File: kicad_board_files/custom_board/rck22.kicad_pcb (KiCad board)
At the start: 2 copper layers, 95.3 x 69.9 mm, 61 parts, among them CON1 Nokia1616_LCD, IC1 PEC11L-4115F-S0020, J1 Conn_02x05_Odd_Even, J2 USB_OTG, J3 Thermocouple, J4 5V_DC_IN, J6 SSR, Q1 BC547, Q2 BSS138, SW1 PTS810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

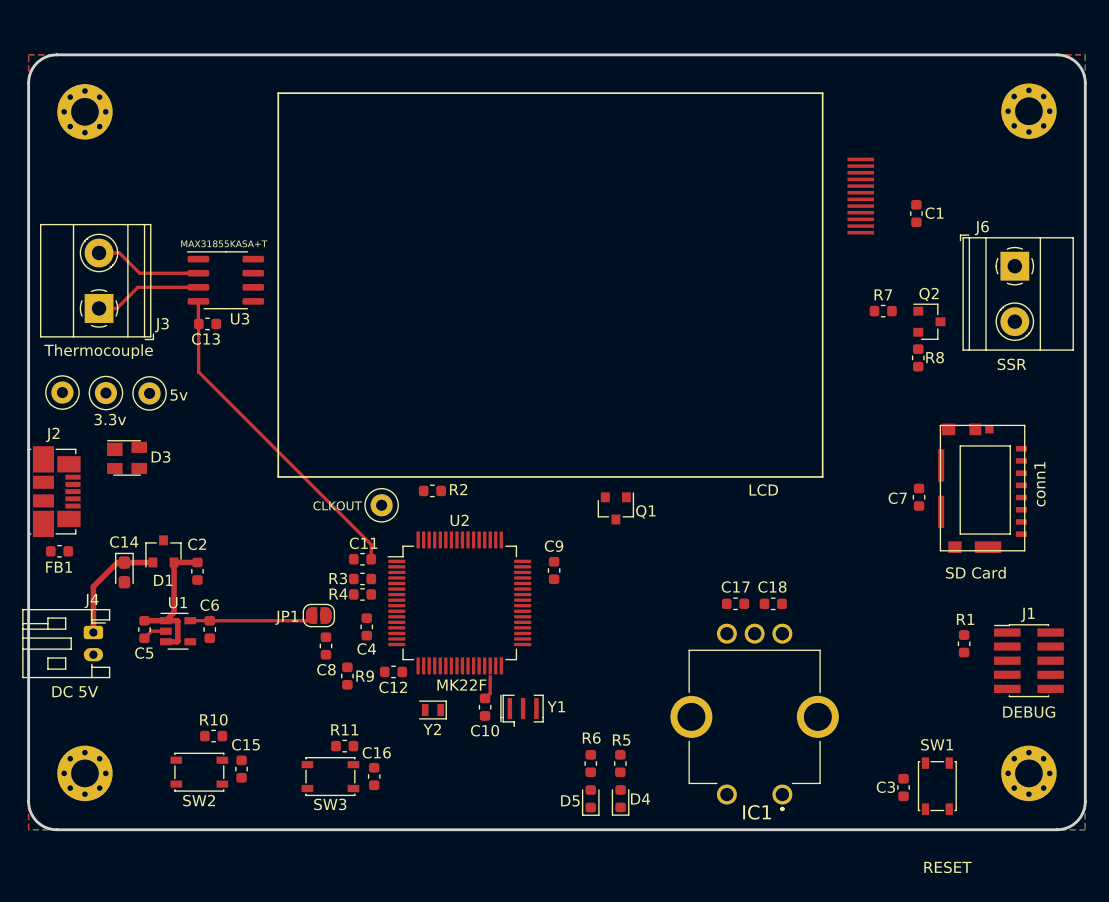
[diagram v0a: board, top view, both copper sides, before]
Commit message: Add protection to thermocouple input
Update the thermocouple interface with ferrite beads and filter capacitor
Add an alternative thermocouple connector other than terminal block
Add extra SSR lines for the case of multiple heaters
Replace the 700mA 3.3V regulator with a 1A regulator, and replace its capacitors
Add 10K series resistors to the rotary encoder ouputs
Replace buttons with two pin header connectors so as to use momentary switches on the casing
Reverse UART connection in ARM SWD debug connector
Tune LED resistors to the datasheet parameters
Rearrange the schamtic and layout
Source all components and generate a HTML BOM
Update the README
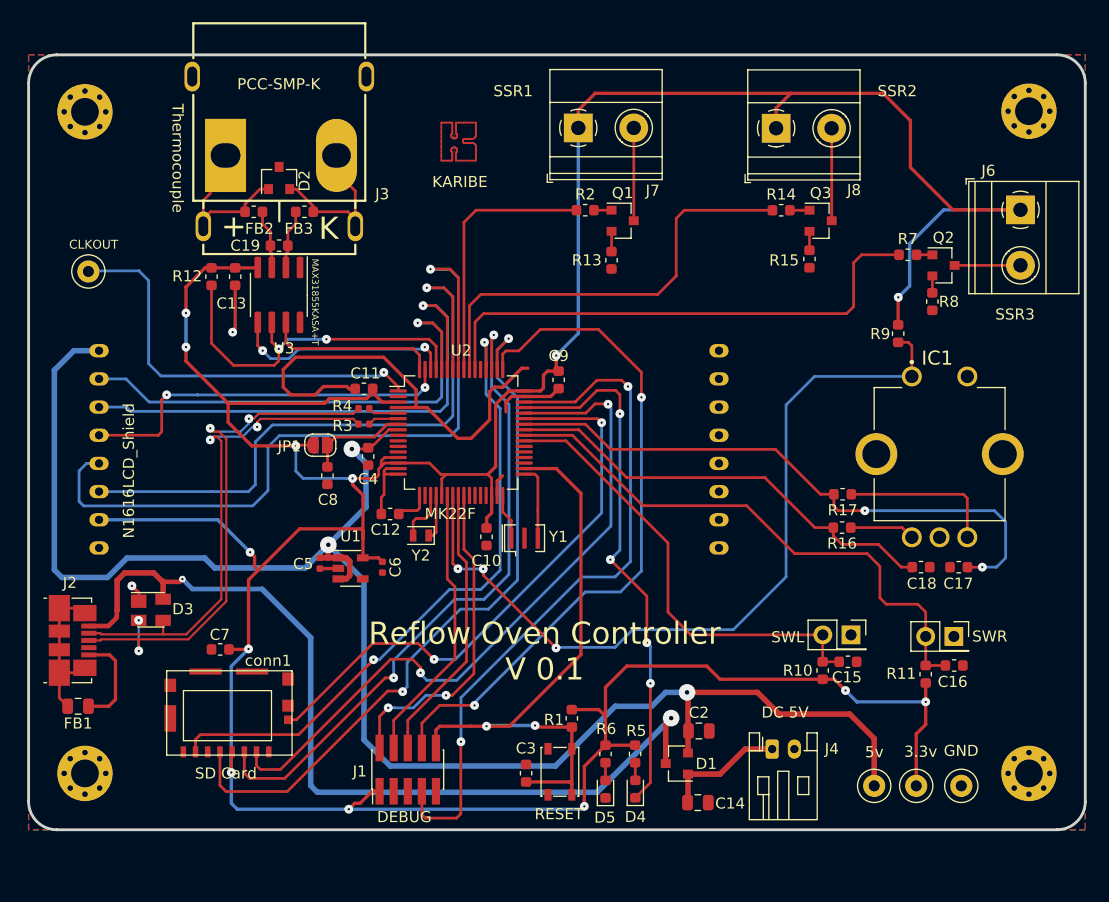
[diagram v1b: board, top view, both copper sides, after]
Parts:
- removed C1: 100nF, Capacitor_SMD:C_0603_1608Metric
- removed CON1: Nokia1616_LCD, LCDs:Nokia1616_LCD_unfolded
- removed SW2, SW3: PTS810, Button_Switch_SMD:SW_SPST_PTS810
- added C19: 10nF/50V/X7R/0603, Capacitor_SMD:C_0603_1608Metric, F.Cu at (115.3, 71.8)
- added D2: NUP2105L, Package_TO_SOT_SMD:SOT-23, F.Cu at (115.3, 65.7)
- added FB2: bead, Inductor_SMD:L_0603_1608Metric, F.Cu at (113.0, 68.8)
- added FB3: bead, Inductor_SMD:L_0603_1608Metric, F.Cu at (117.6, 68.8)
- added J10: Conn_01x02, Connector_PinSocket_2.54mm:PinSocket_2x01_P2.54mm_Vertical, F.Cu at (176.1, 107.0)
- added J5: header, TerminalBlock_Dinkle:TerminalBlock_Dinkle_DT-55-B01X-02_P10.00mm, B.Cu at (110.5, 63.7)
- added J7: SSR, TerminalBlock_Phoenix:TerminalBlock_Phoenix_MKDS-1,5-2_1x02_P5.00mm_Horizontal, F.Cu at (142.3, 61.2)
- added J8: SSR, TerminalBlock_Phoenix:TerminalBlock_Phoenix_MKDS-1,5-2_1x02_P5.00mm_Horizontal, F.Cu at (160.1, 61.2)
- added J9: Conn_01x02, Connector_PinSocket_2.54mm:PinSocket_2x01_P2.54mm_Vertical, F.Cu at (166.8, 106.9)
- added L1: karibe_logo, artwork:karibe_logo, F.Cu at (131.1, 62.5)
- added Q3: BSS138, Package_TO_SOT_SMD:SOT-23, F.Cu at (164.1, 69.6)
- added R12: 10k/0.125W/±1%/0603, Resistor_SMD:R_0603_1608Metric, F.Cu at (109.2, 74.6)
- added R13: 10k/0.125W/±1%/0603, Resistor_SMD:R_0603_1608Metric, F.Cu at (145.3, 73.1)
- added R14: 100, Resistor_SMD:R_0603_1608Metric, F.Cu at (160.5, 68.6)
- added R15: 10k/0.125W/±1%/0603, Resistor_SMD:R_0603_1608Metric, F.Cu at (163.1, 73.0)
- added R16: 10k/0.125W/±1%/0603, Resistor_SMD:R_0603_1608Metric, F.Cu at (166.0, 97.2)
- added R17: 10k/0.125W/±1%/0603, Resistor_SMD:R_0603_1608Metric, F.Cu at (166.1, 94.2)
- added U4: N1616LCD_Shield, connectors:N1616LCD_Shield, F.Cu at (99.1, 81.3)
- C13, C15, C16, C17, C18, C3, C4: value 100nF -> 100nF/50V/0603
- C14: value 10uF -> 10uF/6.3V/±20%/X7R/0805; footprint Capacitor_Tantalum_SMD:CP_EIA-2012-15_AVX-P -> Capacitor_SMD:C_0805_2012Metric
- C2: value 10uF -> 10uF/6.3V/±20%/X7R/0805; footprint Capacitor_SMD:C_0603_1608Metric -> Capacitor_SMD:C_0805_2012Metric
- C5, C6: value 1uF -> 10uF/6.3V/±20%/X7R/0805; footprint Capacitor_SMD:C_0603_1608Metric -> Capacitor_SMD:C_0402_1005Metric
- C7: value 22uF -> 22uF/6.3V/±20%/0603
- FB1: value 330 -> 330Ohm@100MHz; footprint Inductor_SMD:L_0603_1608Metric -> Inductor_SMD:L_0805_2012Metric
- J3: value Thermocouple -> PCC-SMP-K; footprint TerminalBlock_Phoenix:TerminalBlock_Phoenix_MKDS-1,5-2_1x02_P5.00mm_Horizontal -> connectors:PCC-SMP-K
- Q1: value BC547 -> BSS138
- R1, R10, R11, R9: value 10k -> 10k/0.125W/±1%/0603
- R2: value 1k -> 100
- R3, R4: footprint Resistor_SMD:R_0603_1608Metric -> Resistor_SMD:R_0402_1005Metric
- R5: value 1K -> 16.9
- R6: value 1K -> 23.2
- R8: value 10K -> 10k/0.125W/±1%/0603
- TP1, TP3: value (none) -> 5003
- TP2: value (none) -> 5001
- TP4: value (none) -> 5002
- U1: value AP2112K-3.3 -> XC6220B331MR
- moved TP2 88.4 mm to (176.8, 120.5), turned to 270 degrees
- moved TP4 81.2 mm to (172.7, 120.5), turned to 270 degrees
- moved conn1 79.5 mm to (105.2, 117.7), turned to 0 degrees
- moved TP1 74.3 mm to (168.9, 120.5), turned to 270 degrees
- moved C7 64.5 mm to (110.0, 108.2), turned to 180 degrees
- moved J4 62.1 mm to (159.7, 117.2), turned to 0 degrees
- moved R9 58.5 mm to (171.1, 79.7)
- moved J1 56.8 mm to (126.9, 119.0), turned to 90 degrees
- moved C14 55.7 mm to (153.0, 122.0), turned to 0 degrees
- moved C15 55.5 mm to (166.6, 109.3), turned to 0 degrees
- moved R10 55.2 mm to (164.3, 110.1), turned to 90 degrees
- moved C16 53.2 mm to (176.1, 109.7), turned to 0 degrees
- moved R11 52.8 mm to (173.6, 110.4), turned to 90 degrees
- moved D1 50.1 mm to (151.1, 118.5), turned to 180 degrees
- moved C2 47.4 mm to (153.1, 115.6), turned to 0 degrees
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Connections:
- net Net-(D4-Pad1) renamed GREEN
- net Net-(R3-Pad1) renamed /DP
- net Net-(R4-Pad2) renamed /DN
- C15 pad 1: SWR -> SWL
- C16 pad 1: SWL -> SWR
- D3 pad 2: /D- -> /D+
- D3 pad 3: /D+ -> /D-
- IC1 pad A1: ENC_A -> A
- IC1 pad B1: ENC_B -> B
- J3 pad 1: T+ -> Net-(D2-Pad1)
- J3 pad 2: T- -> Net-(D2-Pad2)
- Q1 pad 1: LED- -> Net-(Q1-Pad1)
- Q1 pad 3: GND -> Net-(J7-Pad2)
- R10 pad 2: SWR -> SWL
- R11 pad 2: SWL -> SWR
- R2 pad 1: LCD_PWM -> SSR1_PWM
- R2 pad 2: Net-(Q1-Pad2) -> Net-(Q1-Pad1)
- R7 pad 1: SSR_PWM -> SSR3_PWM
- TP1 pad 1: +5VP -> VREGIN
- U2 pad 54: (no net) -> SSR3_PWM
- U2 pad 55: SSR_PWM -> SSR2_PWM
- U2 pad 56: (no net) -> SSR1_PWM
- U3 pad 2: T- -> Net-(C19-Pad2)
- U3 pad 3: T+ -> Net-(C19-Pad1)
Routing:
- net +3V3: track 43.0 -> 343.1 mm, vias 0 -> 13
- net VREGIN: track 13.6 -> 151.7 mm, vias 0 -> 3
- net +5V: track 0.00 -> 81.4 mm, vias 0 -> 2
- net SW: track 0.00 -> 74.3 mm, vias 0 -> 3
- net LCD_RESET: track 0.00 -> 71.9 mm, vias 0 -> 1
- net SD_CLK: track 0.00 -> 65.5 mm, vias 0 -> 2
- net SD_CS: track 0.00 -> 63.4 mm, vias 0 -> 2
- net GND: track 2.19 -> 65.5 mm, vias 0 -> 2
- net UART_RX: track 0.00 -> 63.0 mm, vias 0 -> 2
- net UART_TX: track 0.00 -> 62.2 mm, vias 0 -> 2
- net SD_MOSI: track 0.00 -> 60.0 mm, vias 0 -> 2
- net LCD_CS: track 0.00 -> 59.7 mm, vias 0 -> 1
- net SD_MISO: track 0.00 -> 58.5 mm, vias 0 -> 2
- net RESET: track 0.00 -> 56.2 mm, vias 0 -> 2
- net ENC_B: track 0.00 -> 54.7 mm, vias 0 -> 2
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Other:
- net class 5v: clearance 0.3 -> 0.2
- net class Default: clearance 0.16 -> 0.12
- net class power: clearance 0.25 -> 0.2
- rule solder_mask_min_width: 0.25 -> 0.08
- rule trace_clearance: 0.16 -> 0.12
- board text added: "GND"
- board text added: "KARIBE"
- board text added: "Reflow Oven Controller V 0.1"
- board text added: "SSR1"
- board text added: "SSR2"
- board text added: "SSR3"
- board text added: "SWL"
- board text added: "SWR"
- board text removed: "LCD"
- board text removed: "SSR"

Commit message: Tweak the PCB silkscreen, add main UI graphic
Add some silkscreen text with version number and Logos
Add a graphic to be loaded from SD card for the main UI before reflow graph
Tweak the PCB layout and export new images from the 3D viewer
Update the README
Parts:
- added R18: 680/±1%/0.1W/0402, Resistor_SMD:R_0402_1005Metric, F.Cu at (122.2, 119.1)
- moved L1 1.52 mm to (129.6, 62.1)
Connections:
- J1 pad 7: UART_RX -> UART_TX
- J1 pad 8: UART_TX -> UART_RX
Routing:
- net UART_RX: track 63.0 -> 54.2 mm
- net UART_TX: track 62.2 -> 70.1 mm
- net SWD_IO: track 29.4 -> 32.6 mm
- net RESET: track 56.2 -> 58.8 mm
- net +3V3: track 343.1 -> 345.7 mm

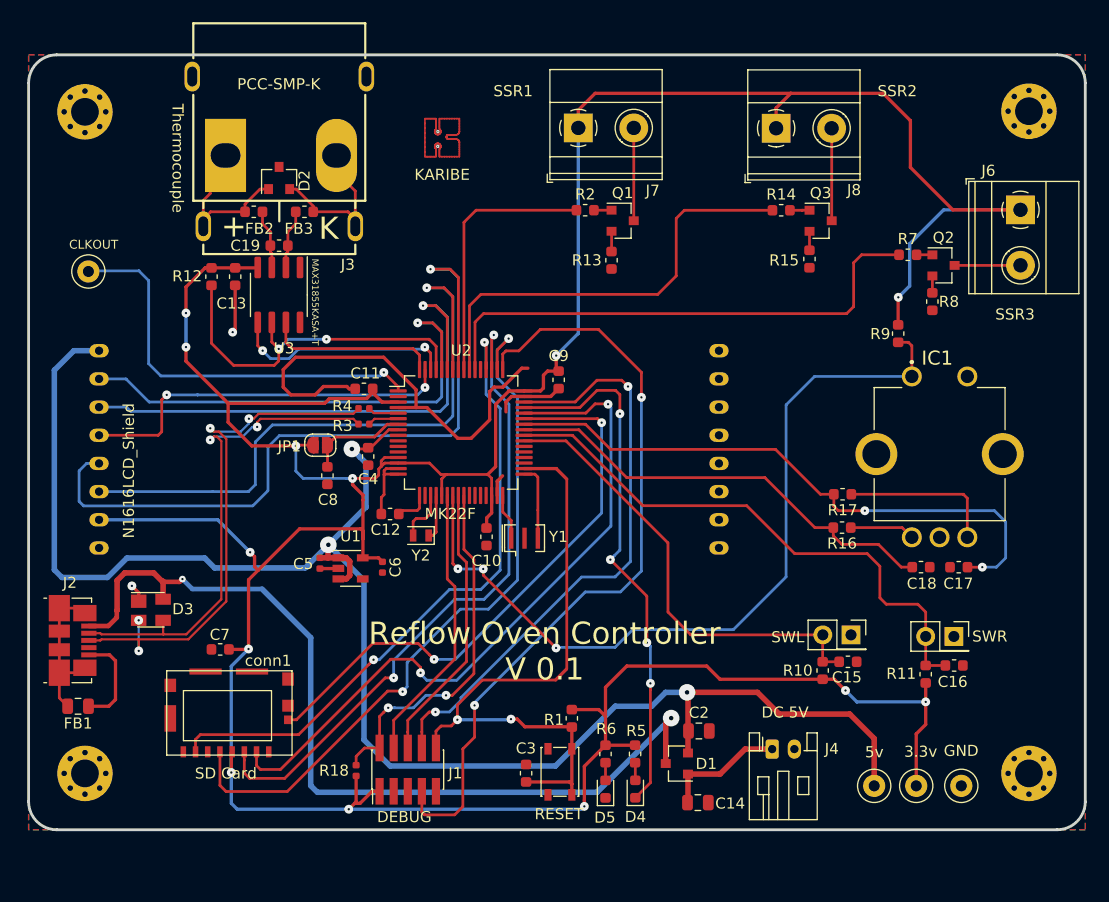
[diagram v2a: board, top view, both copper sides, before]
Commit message: touch up the board
Re-assign some GPIOs to simplify routing
Mark SMD components as surface mount in their properties
Re-arrange power connector and status LEDs
Replace the SD card component with one readily available at LCSC.com
Add optional on-board SMD PTS810 buttons
Change some capacitor footprints from 0402 to 0805 to reduce BOM items
Add more details on the silkscreen: dimensions, jlcpcb customer identifier placeholder e.t.c
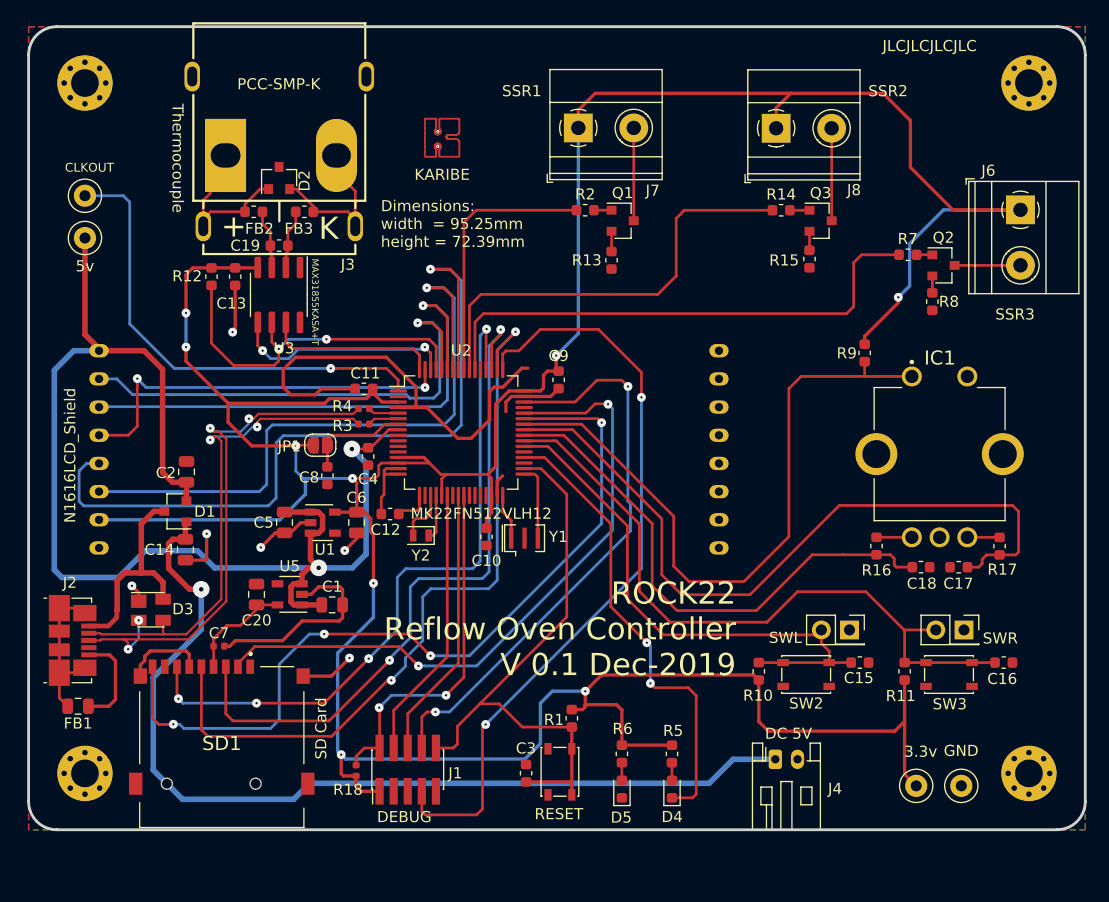
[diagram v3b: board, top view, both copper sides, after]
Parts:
- removed conn1: sdcard_1051620101, connectors:sdcard_1051620101
- added C1: 10uF/6.3V/±20%/X7R/0805, Capacitor_SMD:C_0805_2012Metric, F.Cu at (120.1, 104.2)
- added C20: 10uF/6.3V/±20%/X7R/0805, Capacitor_SMD:C_0805_2012Metric, F.Cu at (113.3, 103.3)
- added SD1: TF-01A, connectors:TF01A, F.Cu at (110.1, 117.0)
- added SW2: PTS810, Button_Switch_SMD:SW_SPST_PTS810, F.Cu at (162.8, 110.5)
- added SW3: PTS810, Button_Switch_SMD:SW_SPST_PTS810, F.Cu at (175.7, 110.5)
- added U5: XC6220B331MR, Package_TO_SOT_SMD:SOT-23-5, F.Cu at (116.2, 103.2)
- C10, C11, C12, C9: value 100nF -> 100nF/50V/0603
- C5, C6: footprint Capacitor_SMD:C_0402_1005Metric -> Capacitor_SMD:C_0805_2012Metric
- C7: value 22uF/6.3V/±20%/0603 -> 100nF/16V/X7R/0402; footprint Capacitor_SMD:C_0603_1608Metric -> Capacitor_SMD:C_0402_1005Metric
- C8: value 2.2uF -> 2.2uF/6.3V/±10%/0603
- moved TP1 86.6 mm to (97.8, 71.1), turned to 0 degrees
- moved C2 51.8 mm to (106.9, 92.2), turned to 90 degrees
- moved C14 51.5 mm to (106.8, 99.2), turned to 270 degrees
- moved D1 50.6 mm to (105.9, 95.8)
- moved R17 14.9 mm to (180.2, 98.9), turned to 270 degrees
- moved TP3 6.83 mm to (97.8, 67.3)
- moved R10 5.76 mm to (158.5, 110.2)
- moved C5 4.86 mm to (115.8, 96.8)
- moved U1 4.83 mm to (119.2, 96.8)
- moved C6 4.65 mm to (122.3, 96.8)
- moved C16 4.48 mm to (180.6, 109.4)
- moved R16 3.52 mm to (169.1, 98.9), turned to 270 degrees
- moved R9 3.49 mm to (168.1, 81.5)
- moved R5 3.32 mm to (150.7, 117.6)
- moved D4 3.30 mm to (150.7, 120.8)
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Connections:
- net Net-(C8-Pad1) renamed VOUT33
- C7 pad 1: +3V3 -> 3v3_SD
- U2 pad 23: SW -> (no net)
- U2 pad 36: (no net) -> GREEN
- U2 pad 38: (no net) -> SWL
- U2 pad 39: SWL -> SWR
- U2 pad 40: SWR -> ENC_A
- U2 pad 41: ENC_A -> ENC_B
- U2 pad 42: ENC_B -> SW
- U2 pad 45: GREEN -> (no net)
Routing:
- net +5VP: track 11.1 -> 86.0 mm, vias 0 -> 1
- net +5V: track 81.4 -> 19.5 mm, vias 2 -> 0
- net GND: track 65.5 -> 106.0 mm, vias 2 -> 6
- net VREGIN: track 151.7 -> 116.2 mm, vias 3 -> 2
- net SD_SW: track 52.5 -> 73.9 mm, vias 2 -> 4
- net SW: track 74.3 -> 60.3 mm, vias 3 -> 0
- net +3V3: track 345.7 -> 332.1 mm, vias 13 -> 9
- net ENC_B: track 54.7 -> 66.3 mm, vias 2 -> 0
- net B: track 14.1 -> 2.93 mm
- net SWR: track 51.1 -> 61.1 mm
- net 3v3_SD: track 0.00 -> 9.79 mm
- net SWL: track 41.7 -> 49.4 mm
- net ENC_A: track 40.6 -> 47.8 mm
- net GREEN: track 48.2 -> 41.9 mm, vias 4 -> 2
- net RESET: track 58.8 -> 52.9 mm, vias 2 -> 0
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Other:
- board size 95.3 x 69.9 mm -> 95.3 x 72.4 mm
- board text added: "Dimensions: width = 95.25mm height = 72.39mm"
- board text added: "JLCJLCJLCJLC"
- board text added: "MK22FN512VLH12"
- board text added: "ROCK22 Reflow Oven Controller V 0.1 Dec-2019"
- board text removed: "MK22F"
- board text removed: "Reflow Oven Controller V 0.1"
